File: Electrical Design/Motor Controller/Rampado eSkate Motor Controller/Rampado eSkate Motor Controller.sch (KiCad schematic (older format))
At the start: 0 parts

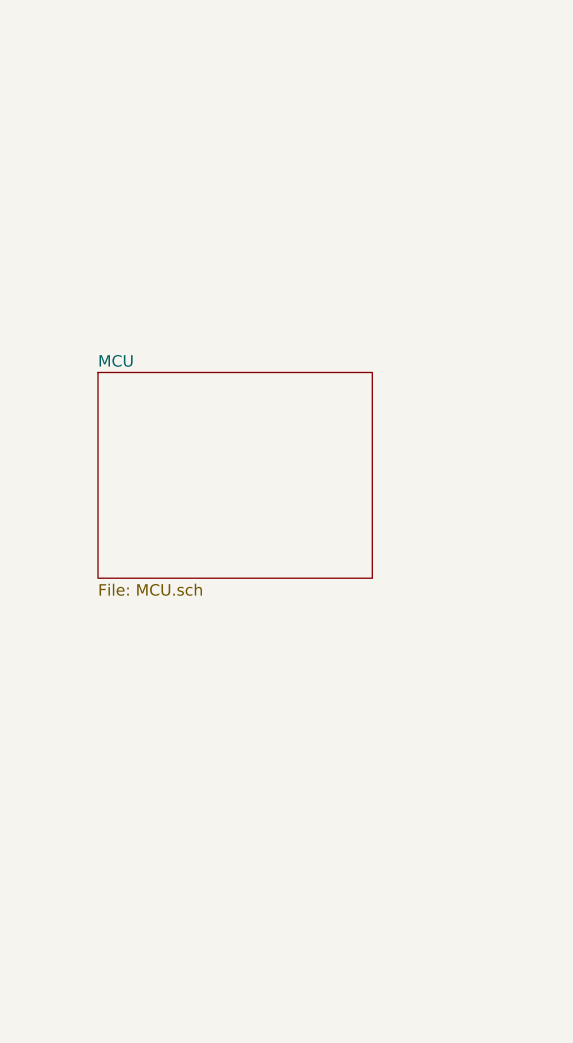
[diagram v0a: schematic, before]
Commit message: Finished USB and started peripherals for motor controller
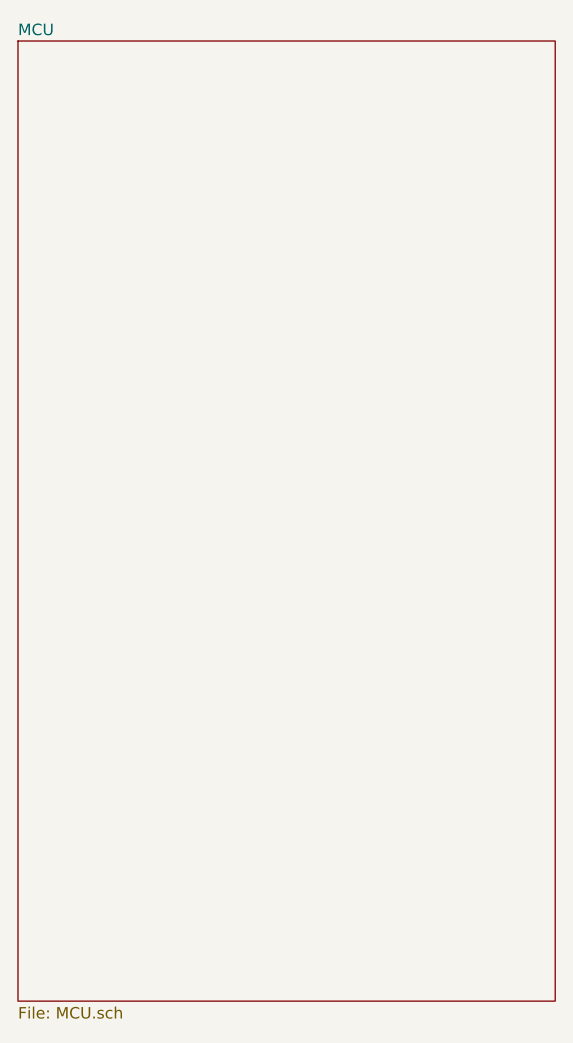
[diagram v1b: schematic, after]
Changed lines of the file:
@@
 $EndDescr
 $Sheet
-S 4900 2600 1200 900
+S 4550 1150 2350 4200
 U 5FA9E78B
 F0 "MCU" 50
